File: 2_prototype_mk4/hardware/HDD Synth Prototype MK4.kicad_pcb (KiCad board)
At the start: 2 copper layers, 100.3 x 69.9 mm, 34 parts, among them J1 Micro_SD_Card, J2 Conn_01x04_Pin, J3 Conn_02x20_Odd_Even, J4 1734451-1, J5 Conn_01x03_Pin, U1 MAX98357A, U2 Optocoupler_DC_PhotoNPN_AKEC

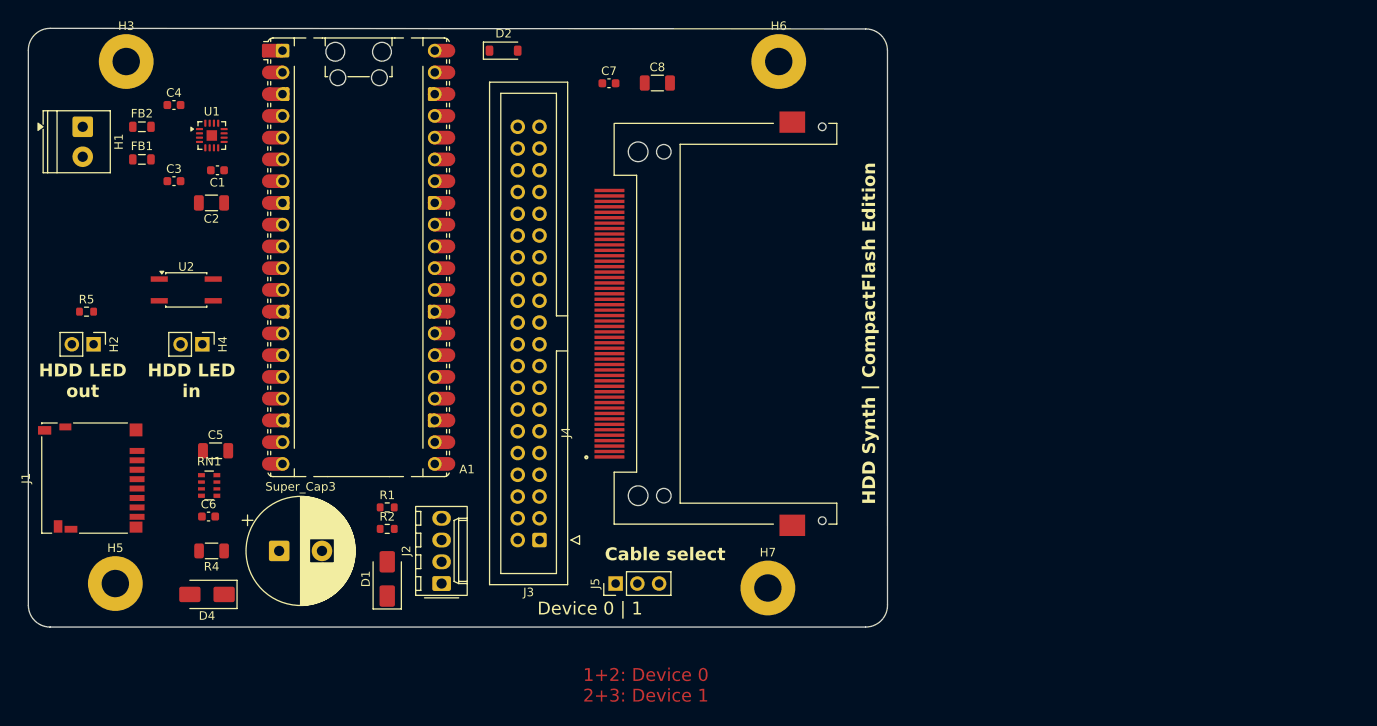
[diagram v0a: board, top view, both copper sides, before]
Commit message: Placed all components on PCB
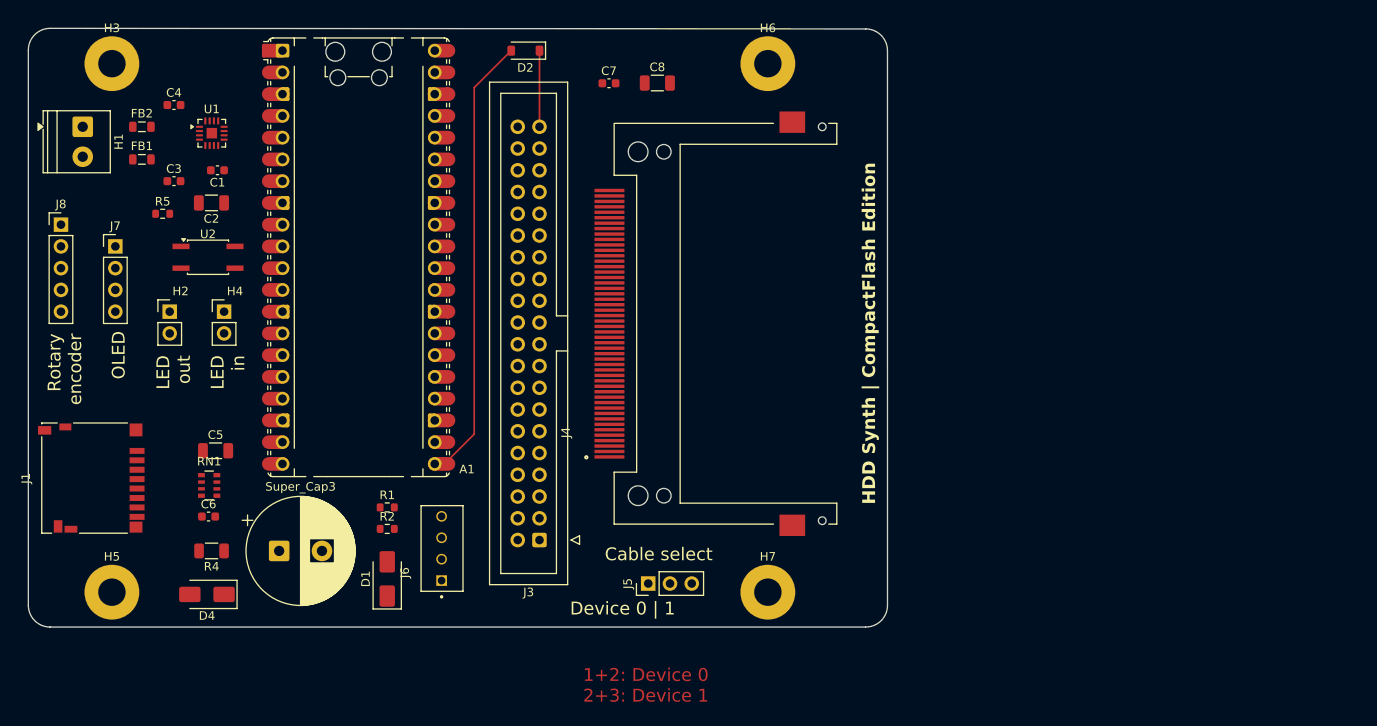
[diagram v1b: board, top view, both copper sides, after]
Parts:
- removed J2: Conn_01x04_Pin, Connector_Molex:Molex_KK-254_AE-6410-04A_1x04_P2.54mm_Vertical
- added J6: 171825-4, Custom:TE_171825-4, F.Cu at (121.9, 111.4)
- added J7: Conn_01x04_Pin, Connector_PinHeader_2.54mm:PinHeader_1x04_P2.54mm_Vertical, F.Cu at (83.8, 72.4)
- added J8: Conn_01x05, Connector_PinHeader_2.54mm:PinHeader_1x05_P2.54mm_Vertical, F.Cu at (77.5, 69.8)
- moved R5 14.5 mm to (89.3, 68.6)
- moved H2 9.67 mm to (90.2, 80.0), turned to 0 degrees
- moved U2 4.58 mm to (94.6, 73.7)
- moved H4 4.58 mm to (96.5, 80.0), turned to 0 degrees
- moved J5 3.81 mm to (146.1, 111.8)
- moved D2 2.54 mm to (131.7, 49.5), turned to 180 degrees
- moved H3 1.69 mm to (83.4, 51.0)
- moved H6 1.29 mm to (160.0, 51.0)
- moved H5 1.09 mm to (83.4, 112.8)
- moved H7 0.49 mm to (160.0, 112.8)
- moved U1 0.27 mm to (95.1, 59.2)
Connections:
- A1 pad 10: unconnected-(A1-GPIO7-Pad10) -> /HDD_LED_IN
- A1 pad 22: unconnected-(A1-GPIO17-Pad22) -> /Rotary encoder/ENC_A
- A1 pad 24: unconnected-(A1-GPIO18-Pad24)_1 -> /Rotary encoder/ENC_B
- A1 pad 25: unconnected-(A1-GPIO19-Pad25) -> /Rotary encoder/ENC_SWITCH
- A1 pad 5: /HDD_LED_OUT -> unconnected-(A1-GPIO3-Pad5)_1
- A1 pad 6: /HDD_LED_IN -> /OLED/OLED_SDA
- A1 pad 7: unconnected-(A1-GPIO5-Pad7)_1 -> /OLED/OLED_SCL
- A1 pad 9: unconnected-(A1-GPIO6-Pad9)_1 -> /HDD_LED_OUT
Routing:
- net /IDE/IDE_ACTIVITY: track 0.00 -> 52.6 mm
- net /IDE/IDE_DASP: track 0.00 -> 8.89 mm
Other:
- board text added: "2.5{dblquote} Drive size 100.35mm (3.95{dblquote}) x 69.85mm (2.75{dblquote})"
- board text added: "LED in"
- board text added: "LED out"
- board text added: "OLED"
- board text added: "Rotary encoder"
- board text removed: "HDD LED in"
- board text removed: "HDD LED out"

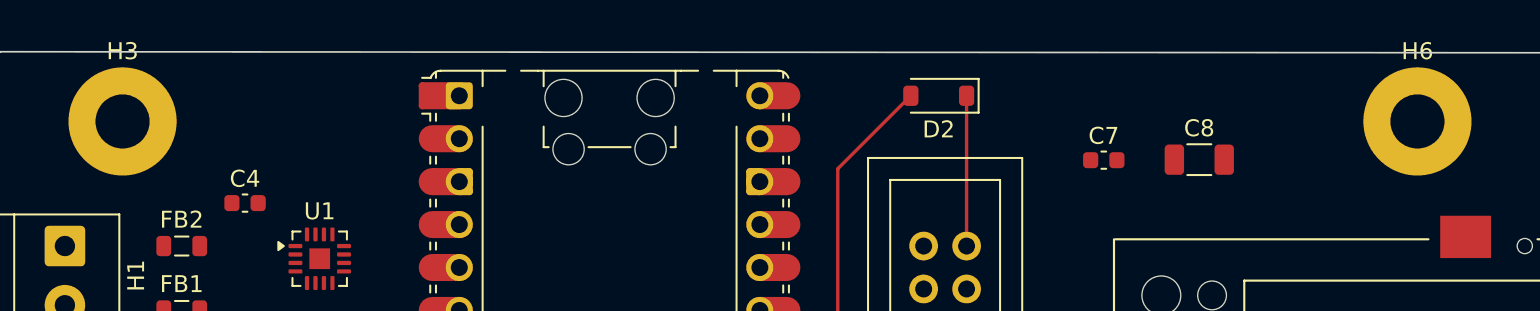
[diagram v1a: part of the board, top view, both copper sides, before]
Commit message: Fixed all Electrical Rule Check errors
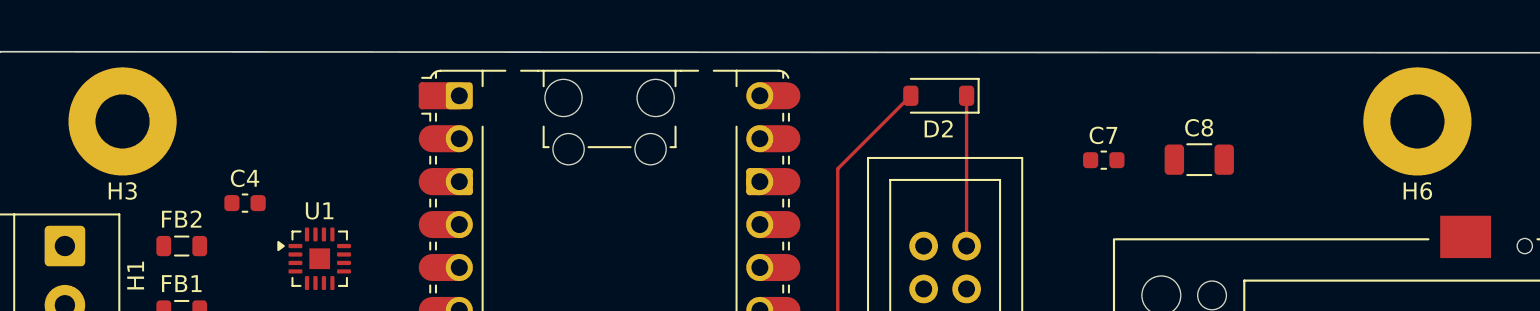
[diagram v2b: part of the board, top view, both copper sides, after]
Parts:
- turned H3 to 180 degrees
- turned H6 to 180 degrees
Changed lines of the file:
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@@
 		(locked yes)
 		(layer "F.Cu")
-		(at 160.02 51.05)
+		(at 160.02 51.05 180)
 		(descr "Mounting Hole 3.2mm, M3, generated by kicad-footprint-generator mountinghole.py")
 		(tags "mountinghole M3")
@@
 		)
 		(pad "1" thru_hole circle
-			(at 0 0)
+			(at 0 0 180)
 			(size 6.4 6.4)
 			(drill 3.2)
@@
 		(locked yes)
 		(layer "F.Cu")
-		(at 83.42 51.05)
+		(at 83.42 51.05 180)
 		(descr "Mounting Hole 3.2mm, M3, generated by kicad-footprint-generator mountinghole.py")
 		(tags "mountinghole M3")
@@
 		)
 		(pad "1" thru_hole circle
-			(at 0 0)
+			(at 0 0 180)
 			(size 6.4 6.4)
 			(drill 3.2)

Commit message: MK4 PCB layout complete
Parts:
- added G***: LOGO, HDDSyncMKIII:MHDDLA_GB_40mm, F.Cu at (217.2, 81.3)
- added G***: LOGO, Custom:MHDDLA_30mm, F.Cu at (163.8, 82.5)
- added G***: LOGO, Custom:HDDSynthLogo_40mm, B.Cu at (158.0, 80.0)
- added R3: 10K, Resistor_SMD:R_0603_1608Metric, F.Cu at (125.7, 79.2)
- added R6: 10K, Resistor_SMD:R_0603_1608Metric, F.Cu at (125.7, 69.8)
- moved C2 16.7 mm to (91.4, 51.0), turned to -90 degrees
- moved C1 12.7 mm to (95.2, 50.8), turned to -90 degrees
- moved C6 9.30 mm to (93.2, 94.8), turned to 90 degrees
- moved J4 4.55 mm to (146.1, 81.9)
- moved R1 2.55 mm to (116.0, 105.4), turned to 180 degrees
- moved R2 2.55 mm to (116.0, 102.9), turned to 180 degrees
- moved C5 2.48 mm to (97.8, 95.2), turned to 90 degrees
- moved FB1 0.35 mm to (86.6, 62.2), turned to 180 degrees
- moved FB2 0.35 mm to (86.6, 58.4), turned to 180 degrees
- turned C4 to 180 degrees
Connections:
- A1 pad 39: /Power/5V_POWER -> POWER_5V_SUP
- D1 pad 1: /Power/5V_POWER -> POWER_5V_SUP
- D4 pad 1: /Power/5V_POWER -> POWER_5V_SUP
- J4 pad 43: unconnected-(J4-Pad43) -> /IDE/IDE_DMARQ
- J4 pad 44: +3.3V -> /IDE/IDE_DMACK
- R4 pad 1: /Power/5V_POWER -> POWER_5V_SUP
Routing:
- net +3.3V: track 0.00 -> 188.3 mm, vias 0 -> 6
- net POWER_5V_SUP: track 0.00 -> 141.2 mm
- net GND: track 0.00 -> 67.8 mm, vias 0 -> 18
- net /Rotary encoder/ENC_A: track 0.00 -> 59.7 mm
- net /IDE/CF_CABLE_SELECT: track 0.00 -> 56.3 mm, vias 0 -> 3
- net /Rotary encoder/ENC_B: track 0.00 -> 51.3 mm, vias 0 -> 1
- net /Rotary encoder/ENC_SWITCH: track 0.00 -> 47.9 mm
- net /VCC_DETECT: track 0.00 -> 47.6 mm, vias 0 -> 1
- net /IDE/IDE_RESET: track 0.00 -> 45.4 mm
- net /IDE/IDE_CHIPSELECT_1: track 0.00 -> 42.9 mm, vias 0 -> 1
- net /IDE/D08: track 0.00 -> 42.4 mm
- net /IDE/IDE_CHIPSELECT_0: track 0.00 -> 41.7 mm, vias 0 -> 1
- net /IDE/D09: track 0.00 -> 41.2 mm
- net /IDE/D10: track 0.00 -> 39.9 mm
- net /IDE/D00: track 0.00 -> 38.5 mm
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- added copper zone on B.Cu, net GND
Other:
- board text added: "CompactFlash Edition | Prototype MK4"
- board text added: "Special thanks to: - Cecilia MacLoughlin - Ian (polpo) Scott - Ian (PSYCHROME) Ball - Mark Angus - Neil Thomas (Retro Collective) - vswitchzero - Wouter Groeneveld - VOGONS and SWAG"
- board text removed: "HDD Synth | CompactFlash Edition"

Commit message: Final design to sent to PCBWay
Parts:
- removed the G*** at (217.2, 81.3)
- removed R6: 10K, Resistor_SMD:R_0603_1608Metric
- R3: value 10K -> 4.7K
- R4: footprint Resistor_SMD:R_1206_3216Metric -> Resistor_SMD:R_0603_1608Metric
- moved R3 14.9 mm to (126.0, 64.3), turned to 0 degrees
- moved D2 10.4 mm to (127.0, 58.8), turned to -90 degrees
- moved C7 6.48 mm to (147.8, 54.6)
- moved J3 2.84 mm to (135.9, 105.4)
- moved C8 2.81 mm to (148.4, 50.8)
- moved J4 0.26 mm to (146.3, 82.0)
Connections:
- C7 pad 1: +3.3V -> POWER_5V_SUP
- C8 pad 1: +3.3V -> POWER_5V_SUP
- J3 pad 11: /IDE/D04 -> /IDE/D03
- J3 pad 13: /IDE/D05 -> /IDE/D02
- J3 pad 15: /IDE/D06 -> /IDE/D01
- J3 pad 17: /IDE/D07 -> /IDE/D00
- J3 pad 21: /IDE/IDE_DMARQ -> unconnected-(J3-Pin_21-Pad21)
- J3 pad 29: /IDE/IDE_DMACK -> unconnected-(J3-Pin_29-Pad29)
- J3 pad 3: /IDE/D00 -> /IDE/D07
- J3 pad 5: /IDE/D01 -> /IDE/D06
- J3 pad 7: /IDE/D02 -> /IDE/D05
- J3 pad 9: /IDE/D03 -> /IDE/D04
- J4 pad 10: unconnected-(J4-Pad10) -> GND
- J4 pad 11: unconnected-(J4-Pad11) -> GND
- J4 pad 12: unconnected-(J4-Pad12) -> GND
- J4 pad 13: +3.3V -> POWER_5V_SUP
- J4 pad 14: unconnected-(J4-Pad14) -> GND
- J4 pad 15: unconnected-(J4-Pad15) -> GND
- J4 pad 16: unconnected-(J4-Pad16) -> GND
- J4 pad 17: unconnected-(J4-Pad17) -> GND
- J4 pad 33: unconnected-(J4-Pad33) -> GND
- J4 pad 36: +3.3V -> unconnected-(J4-Pad36)
- J4 pad 38: +3.3V -> POWER_5V_SUP
- J4 pad 43: /IDE/IDE_DMARQ -> unconnected-(J4-Pad43)
- J4 pad 44: /IDE/IDE_DMACK -> POWER_5V_SUP
- J4 pad 8: unconnected-(J4-Pad8) -> GND
- R3 pad 1: /IDE/IDE_DMARQ -> +3.3V
- R3 pad 2: GND -> /IDE/IDE_ACTIVITY
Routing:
- net +3.3V: track 188.3 -> 98.7 mm, vias 6 -> 3
- net POWER_5V_SUP: track 141.2 -> 217.0 mm, vias 0 -> 4
- net /IDE/CF_CABLE_SELECT: track 56.3 -> 97.9 mm, vias 3 -> 1
- net GND: track 67.8 -> 95.0 mm, vias 18 -> 19
- net /IDE/IDE_DMARQ: track 27.0 -> 0.00 mm, vias 3 -> 0
- net /IDE/D04: track 36.6 -> 11.3 mm
- net /IDE/D03: track 37.1 -> 11.9 mm, vias 1 -> 0
- net /IDE/D11: track 38.2 -> 14.5 mm, vias 1 -> 2
- net /IDE/D13: track 37.1 -> 14.1 mm, vias 2 -> 0
- net /IDE/D15: track 37.7 -> 15.2 mm
- net /IDE/IDE_DMACK: track 22.1 -> 0.00 mm, vias 2 -> 0
- net /IDE/D14: track 36.6 -> 14.7 mm, vias 1 -> 0
- net /IDE/D12: track 35.0 -> 14.5 mm, vias 2 -> 0
- net /IDE/D07: track 36.8 -> 17.5 mm
- net /IDE/D05: track 37.8 -> 19.1 mm, vias 1 -> 0
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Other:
- board text removed: "Cable select"

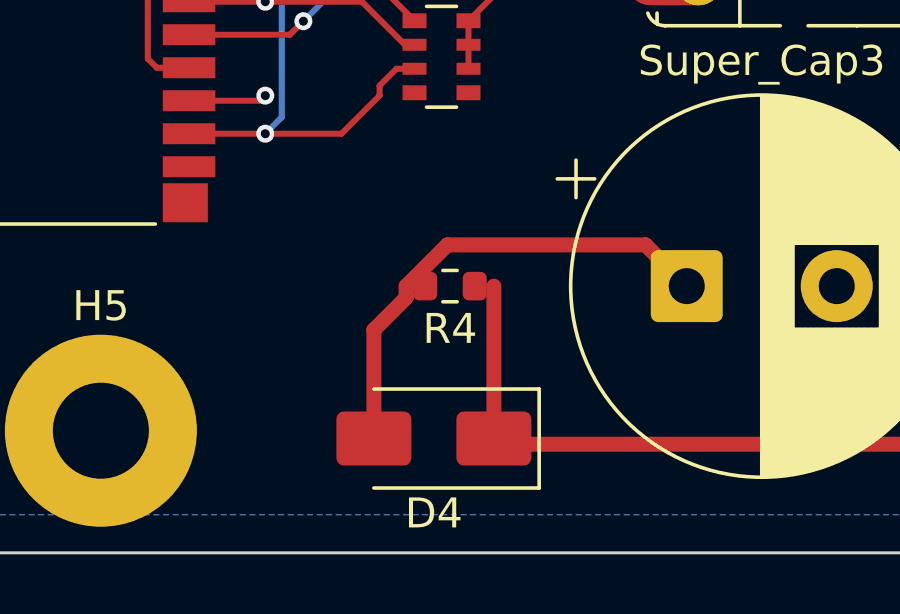
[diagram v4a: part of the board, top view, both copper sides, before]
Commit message: Update MKIV hardware & use MKIII software as basic for MKIV
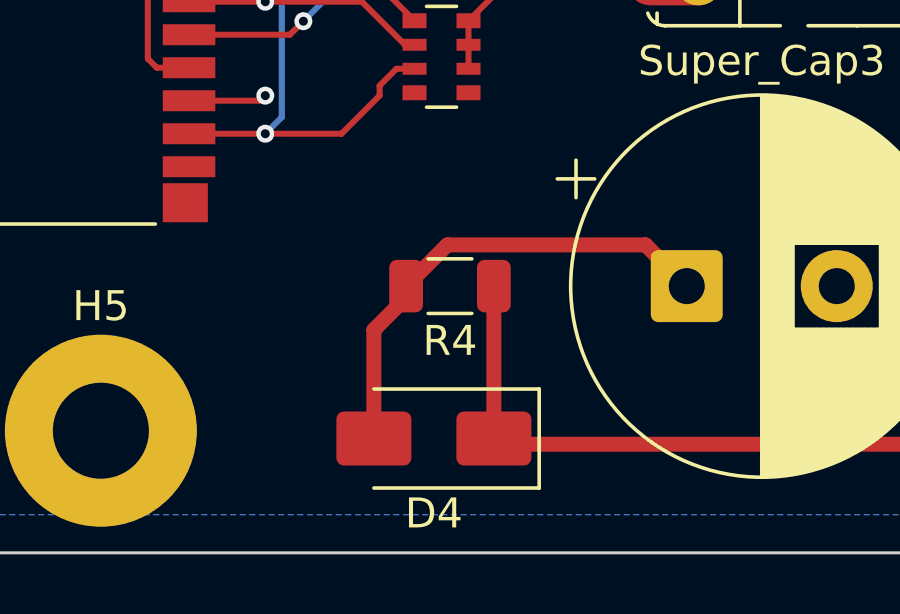
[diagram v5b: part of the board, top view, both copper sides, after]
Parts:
- removed the G*** at (158.0, 80.0)
- added G***: LOGO, Custom:HDDSynthLogoS_MKIV_40mm, B.Cu at (155.2, 79.3)
- R4: footprint Resistor_SMD:R_0603_1608Metric -> Resistor_SMD:R_1206_3216Metric
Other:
- board text added: "CompactFlash Edition"
- board text added: "Peter Bridger www.strifestreams.com/hddsynth"
- board text removed: "CompactFlash Edition | Prototype MK4"

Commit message: Final MKIV tweaks before sending off to PCBWay
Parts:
- removed the G*** at (163.8, 82.5)
- added C10: 100nF, Capacitor_SMD:C_0402_1005Metric, F.Cu at (124.5, 80.0)
- added C9: 100nF, Capacitor_SMD:C_0402_1005Metric, F.Cu at (127.0, 80.0)
- added G***: LOGO, Custom:MHDDLA_21mm, F.Cu at (166.4, 82.5)
- added H8: Conn_01x02, Connector_PinHeader_2.54mm:PinHeader_1x02_P2.54mm_Vertical, F.Cu at (80.0, 81.3)
- added R6: 10K, Resistor_SMD:R_0402_1005Metric, F.Cu at (127.0, 70.6)
- added U3: TXS0101DBV, Package_TO_SOT_SMD:SOT-23-6, F.Cu at (127.1, 75.2)
- Super_Cap3: value 0.47F -> 1F; footprint Capacitor_THT:CP_Radial_D12.5mm_P5.00mm -> Capacitor_THT:CP_Radial_D14.0mm_P5.00mm
- moved J1 27.9 mm to (107.1, 109.4), turned to 180 degrees
- moved D4 26.7 mm to (96.0, 86.4)
- moved Super_Cap3 23.4 mm to (82.5, 96.5)
- moved R4 15.3 mm to (97.8, 92.9), turned to -90 degrees
- moved RN1 10.3 mm to (96.9, 110.4), turned to 180 degrees
- moved C5 10.2 mm to (96.5, 105.4), turned to 180 degrees
- moved J8 10.2 mm to (87.6, 68.6), turned to -90 degrees
- moved C6 8.52 mm to (98.3, 101.6), turned to 180 degrees
- moved R5 6.84 mm to (91.9, 74.9)
- moved U2 5.98 mm to (97.8, 68.6), turned to 90 degrees
- moved J7 2.84 mm to (85.1, 74.9), turned to -90 degrees
- moved D1 2.54 mm to (118.1, 111.2)
- moved J6 2.54 mm to (124.5, 111.4)
- moved R1 2.10 mm to (118.1, 105.4)
- moved R2 2.09 mm to (118.1, 102.9)
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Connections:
- net /IDE/IDE_RESET renamed /IDE_RESET
- A1 pad 26: unconnected-(A1-GPIO20-Pad26)_1 -> /ACTION_BTN
- A1 pad 30: unconnected-(A1-RUN-Pad30)_1 -> /Reset/PICO_RUN
- A1 pad 5: unconnected-(A1-GPIO3-Pad5)_1 -> /Amplifer/SD_MODE
- D1 pad 2: +5V -> POWER_5V_SUP
- J6 pad 1: +5V -> POWER_5V_SUP
- R1 pad 2: +5V -> POWER_5V_SUP
- U1 pad 4: POWER_5V_SUP -> /Amplifer/SD_MODE
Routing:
- net POWER_5V_SUP: track 217.0 -> 268.7 mm, vias 4 -> 6
- net /ACTION_BTN: track 0.00 -> 43.6 mm, vias 0 -> 1
- net /IDE_RESET: track 40.7 -> 80.0 mm, vias 2 -> 3
- net +3.3V: track 98.7 -> 121.6 mm, vias 3 -> 1
- net GND: track 95.0 -> 117.6 mm
- net /Amplifer/SD_MODE: track 0.00 -> 16.6 mm, vias 0 -> 2
- net Net-(D4-A): track 16.0 -> 27.5 mm
- net +5V: track 11.3 -> 0.00 mm
- net /IDE/IDE_ACTIVITY: track 40.4 -> 51.0 mm, vias 0 -> 2
- net /Rotary encoder/ENC_SWITCH: track 47.9 -> 57.0 mm, vias 0 -> 3
- net /Rotary encoder/ENC_A: track 59.7 -> 52.0 mm, vias 0 -> 3
- net /SD card reader/SD_MISO: track 33.8 -> 40.9 mm
- net /HDD_LED_OUT: track 13.7 -> 20.0 mm
- net /Reset/PICO_RUN: track 0.00 -> 5.14 mm
- net /SD card reader/SD_CS: track 25.6 -> 30.8 mm, vias 2 -> 4
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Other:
- board text added: "Button"
